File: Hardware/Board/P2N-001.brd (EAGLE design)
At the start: 72 x 72 mm, 34 parts, among them IC1 4053N, IC2 LTC485N, IC3 74LS07N, IC4 LTC485N, K1 G5V1, T1 2SC1815

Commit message: Update document.
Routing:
- net N$22: track 75.4 -> 154.5 mm, vias 5 -> 0
- net N$10: track 143.2 -> 82.9 mm, vias 4 -> 7
- net N$9: track 120.3 -> 61.2 mm, vias 3 -> 2
- net N$11: track 133.1 -> 76.8 mm, vias 3 -> 5
- net N$1: track 61.1 -> 114.4 mm, vias 1 -> 3
- net N$25: track 135.3 -> 86.6 mm, vias 2 -> 3
- net ANLG2: track 95.3 -> 52.4 mm, vias 3 -> 1
- net N$29: track 142.8 -> 107.0 mm, vias 4 -> 2
- net GND: track 333.4 -> 368.5 mm, vias 0 -> 1
- net MIDI11: track 115.8 -> 83.3 mm, vias 2 -> 3
- net N$27: track 53.4 -> 76.1 mm, vias 2 -> 1
- net N$33: track 71.3 -> 92.4 mm, vias 2 -> 4
- net N$28: track 89.5 -> 110.3 mm, vias 3 -> 2
- net ANLG1: track 57.9 -> 78.3 mm, vias 1 -> 3
- net N$19: track 80.7 -> 100.5 mm, vias 2 -> 3
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
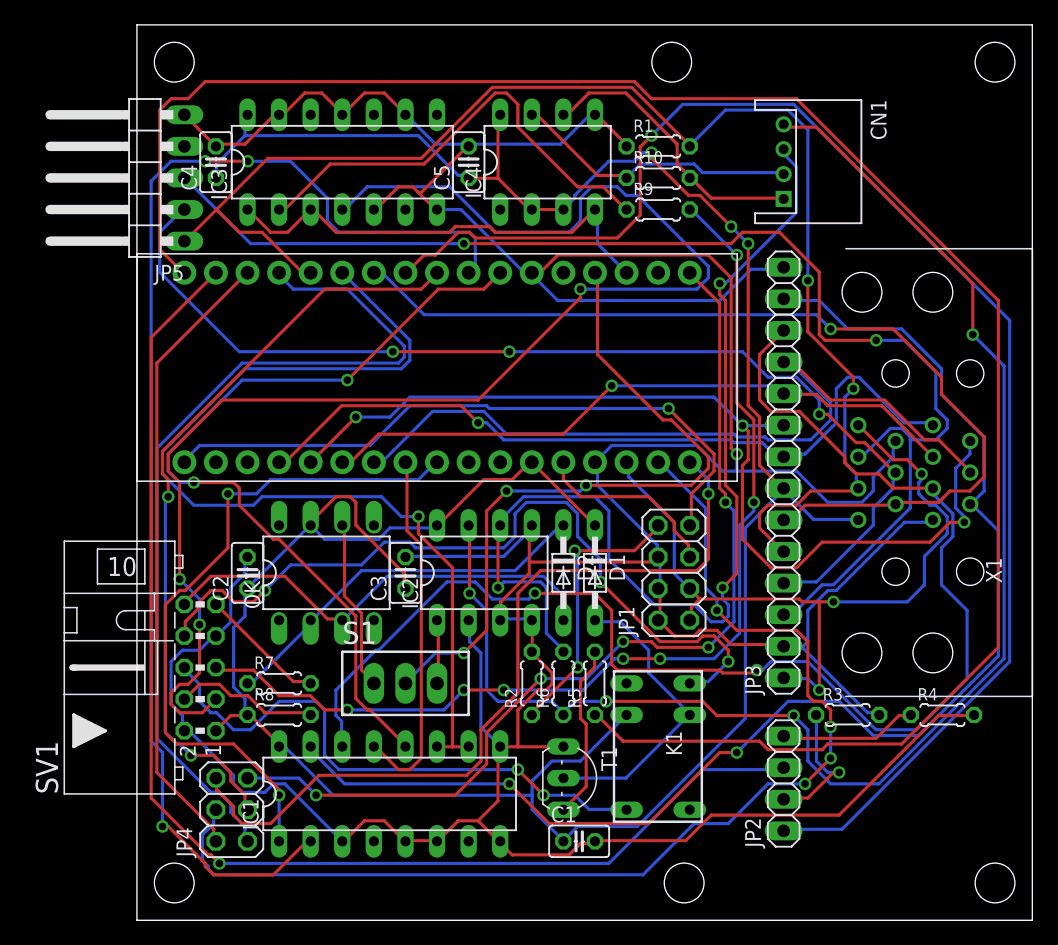
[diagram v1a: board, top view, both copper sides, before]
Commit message: Modified pinout.
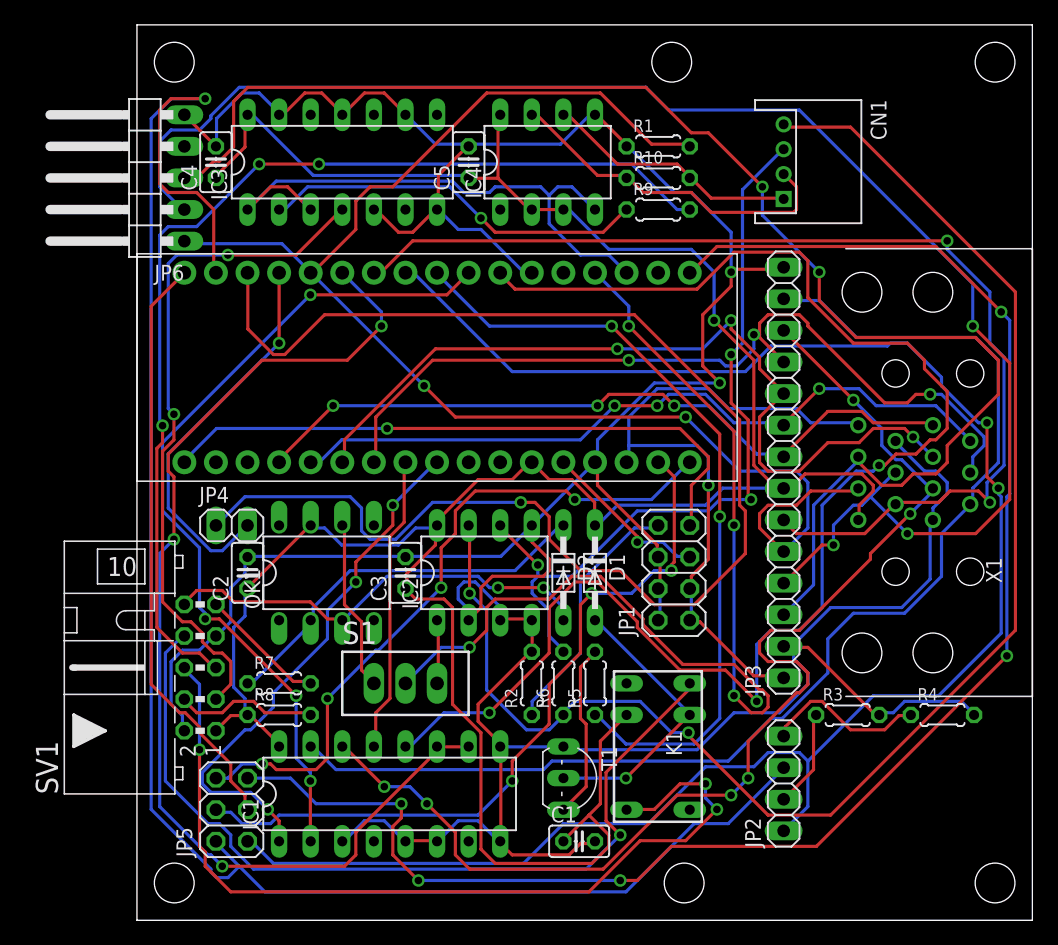
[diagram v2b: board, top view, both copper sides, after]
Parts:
- added JP6: (no value), pinhead:1X05/90
- JP4: device pinhead:2X03 -> pinhead:1X02
- JP5: device pinhead:1X05/90 -> pinhead:2X03
- moved JP5 51.4 mm to (7.62, 8.89)
- moved JP4 22.9 mm to (7.62, 31.8), turned to 0 degrees
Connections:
- removed net N$31: JP4.2, MC1.P$3
- new net N$34: MC1.P$9, R5.1
- net GND: now also JP6.5; no longer JP5.5
- net N$11: now also JP5.5; no longer JP4.5
- net N$13: now also JP5.6; no longer JP4.6
- net N$20: now also JP5.1
- net N$21: now also JP5.2
- net N$22: now also JP4.1, MC1.P$3; no longer MC1.P$1, R5.1
- net N$24: now also JP6.1; no longer JP5.1
- net N$25: now also JP6.2; no longer JP5.2
- net N$26: now also JP6.3; no longer JP5.3
- net N$30: now also JP4.2; no longer JP4.1
- net N$33: now also JP5.4; no longer JP4.4
- net N$9: now also JP5.3, MC1.P$1; no longer JP4.3, MC1.P$9
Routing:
- net N$34: track 0.00 -> 62.8 mm, vias 0 -> 2
- net N$1: track 114.4 -> 55.0 mm, vias 3 -> 2
- net N$11: track 76.8 -> 131.5 mm
- net N$23: track 67.1 -> 119.6 mm, vias 2 -> 3
- net N$31: track 50.8 -> 0.00 mm
- net GND: track 368.5 -> 323.5 mm, vias 1 -> 2
- net N$21: track 100.6 -> 142.4 mm
- net N$22: track 154.5 -> 114.1 mm, vias 0 -> 1
- net N$30: track 71.5 -> 31.3 mm, vias 0 -> 1
- net N$25: track 86.6 -> 126.0 mm
- net N$19: track 100.5 -> 67.9 mm, vias 3 -> 4
- net N$33: track 92.4 -> 60.1 mm, vias 4 -> 3
- net N$20: track 116.2 -> 147.5 mm, vias 1 -> 2
- net N$16: track 45.2 -> 71.0 mm, vias 2 -> 3
- net N$7: track 57.1 -> 81.1 mm, vias 3 -> 4
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
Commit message: Labeled wires.
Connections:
- net GEEK16 renamed SEL
- net MIDI1 renamed TX+
- net MIDI11 renamed RX+
- net MIDI13 renamed RX-
- net MIDI15 renamed RXK
- net MIDI3 renamed TX-
- net MIDI6 renamed TX
- net N$1 renamed RAWTX
- net N$10 renamed RETURN
- net N$11 renamed MOSI
- net N$12 renamed SEND
- net N$13 renamed SCLK
- net N$14 renamed CB
- net N$16 renamed CA
- net N$19 renamed SCL
- net N$20 renamed GPIO0
- net N$21 renamed GPIO1
- net N$22 renamed SX
- net N$23 renamed SDA
- net N$24 renamed PD
- net N$25 renamed USBD-
- net N$26 renamed USBD+
- net N$27 renamed CD
- net N$3 renamed RST
- net N$30 renamed SY
- net N$33 renamed MISO
- net N$34 renamed RELAY
- net N$4 renamed LED
- net N$5 renamed RXA
- net N$7 renamed RX
- net N$9 renamed GPIO2
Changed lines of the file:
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@@
 <via x="27.6606" y="56.4642" extent="1-16" drill="0.6096"/>
 </signal>
-<signal name="MIDI1">
+<signal name="TX+">
 <contactref element="IC4" pad="6"/>
 <contactref element="R10" pad="2"/>
@@
 <wire x1="36.8046" y1="21.4884" x2="36.83" y2="21.59" width="0.254" layer="1"/>
 </signal>
-<signal name="N$1">
+<signal name="RAWTX">
 <contactref element="IC3" pad="4"/>
 <contactref element="SV1" pad="3"/>
@@
 <contactref element="IC1" pad="7"/>
 </signal>
-<signal name="GEEK16">
+<signal name="SEL">
 <contactref element="IC1" pad="11"/>
 <contactref element="IC1" pad="10"/>
@@
 <via x="19.6596" y="47.7774" extent="1-16" drill="0.6096"/>
 </signal>
-<signal name="MIDI6">
+<signal name="TX">
 <contactref element="IC3" pad="1"/>
 <contactref element="IC3" pad="3"/>
@@
 <wire x1="14.1732" y1="24.2316" x2="13.97" y2="24.13" width="0.254" layer="16"/>
 </signal>
-<signal name="MIDI15">
+<signal name="RXK">
 <contactref element="OK1" pad="3"/>
 <contactref element="D2" pad="A"/>
@@
 <via x="29.0322" y="26.7462" extent="1-16" drill="0.6096"/>
 </signal>
-<signal name="MIDI11">
+<signal name="RX+">
 <contactref element="IC2" pad="6"/>
 <contactref element="R6" pad="2"/>
@@
 <via x="32.2326" y="28.575" extent="1-16" drill="0.6096"/>
 </signal>
-<signal name="MIDI13">
+<signal name="RX-">
 <contactref element="IC2" pad="7"/>
 <contactref element="R6" pad="1"/>
@@
 <via x="26.7462" y="26.289" extent="1-16" drill="0.6096"/>
 </signal>
-<signal name="MIDI3">
+<signal name="TX-">
 <contactref element="IC4" pad="7"/>
 <contactref element="R10" pad="1"/>
@@
 <wire x1="39.3192" y1="59.8932" x2="39.37" y2="59.69" width="0.254" layer="1"/>
 </signal>
-<signal name="N$3">
+<signal name="RST">
 <contactref element="JP1" pad="5"/>
 <contactref element="MC1" pad="P$13"/>
@@
 <via x="40.2336" y="30.4038" extent="1-16" drill="0.6096"/>
 </signal>
-<signal name="N$4">
+<signal name="LED">
 <contactref element="JP1" pad="7"/>
 <contactref element="MC1" pad="P$34"/>
@@
 <via x="20.574" y="33.3756" extent="1-16" drill="0.6096"/>
 </signal>
-<signal name="N$10">
+<signal name="RETURN">
 <contactref element="R9" pad="2"/>
 <contactref element="SV1" pad="5"/>
@@
 <via x="2.0574" y="39.7764" extent="1-16" drill="0.6096"/>
 </signal>
-<signal name="N$12">
+<signal name="SEND">
 <contactref element="R8" pad="2"/>
 <contactref element="SV1" pad="4"/>
@@
 <wire x1="3.8862" y1="17.6022" x2="3.81" y2="17.78" width="0.254" layer="1"/>
 </signal>
-<signal name="N$14">
+<signal name="CB">
 <contactref element="K1" pad="10"/>
 <contactref element="SV1" pad="8"/>
@@
 <via x="38.862" y="6.858" extent="1-16" drill="0.6096"/>
 </signal>
-<signal name="N$16">
+<signal name="CA">
 <contactref element="K1" pad="5"/>
 <contactref element="SV1" pad="6"/>
@@
 <via x="5.0292" y="13.716" extent="1-16" drill="0.6096"/>
 </signal>
-<signal name="N$20">
+<signal name="GPIO0">
 <contactref element="MC1" pad="P$8"/>
 <contactref element="JP2" pad="1"/>
@@
 <via x="69.2658" y="34.7472" extent="1-16" drill="0.6096"/>
 </signal>
-<signal name="N$21">
+<signal name="GPIO1">
 <contactref element="MC1" pad="P$2"/>
 <contactref element="JP2" pad="3"/>
@@
 <via x="5.4864" y="66.0654" extent="1-16" drill="0.6096"/>
 </signal>
-<signal name="N$19">
+<signal name="SCL">
 <contactref element="IC1" pad="2"/>
 <contactref element="MC1" pad="P$10"/>
@@
 <via x="13.9446" y="50.292" extent="1-16" drill="0.6096"/>
 </signal>
-<signal name="N$23">
+<signal name="SDA">
 <contactref element="MC1" pad="P$11"/>
 <contactref element="IC1" pad="12"/>
@@
 <via x="59.6646" y="36.576" extent="1-16" drill="0.6096"/>
 </signal>
-<signal name="N$24">
+<signal name="PD">
 <contactref element="X1" pad="5"/>
 <contactref element="JP6" pad="1"/>
@@
 <via x="23.0886" y="42.9768" extent="1-16" drill="0.6096"/>
 </signal>
-<signal name="N$25">
+<signal name="USBD-">
 <contactref element="X1" pad="4"/>
 <contactref element="JP6" pad="2"/>
@@
 <via x="61.9506" y="31.0896" extent="1-16" drill="0.6096"/>
 </signal>
-<signal name="N$26">
+<signal name="USBD+">
 <contactref element="X1" pad="3"/>
 <contactref element="JP6" pad="3"/>
@@
 <via x="54.864" y="52.1208" extent="1-16" drill="0.6096"/>
 </signal>
-<signal name="N$27">
+<signal name="CD">
 <contactref element="X1" pad="6"/>
 <contactref element="JP3" pad="6"/>
@@
 <wire x1="41.8338" y1="31.5468" x2="41.91" y2="31.75" width="0.254" layer="16"/>
 </signal>
-<signal name="N$5">
+<signal name="RXA">
 <contactref element="R7" pad="2"/>
 <contactref element="SV1" pad="9"/>
@@
 <wire x1="6.4008" y1="25.3746" x2="6.35" y2="25.4" width="0.254" layer="1"/>
 </signal>
-<signal name="N$7">
+<signal name="RX">
 <contactref element="S1" pad="2"/>
 <contactref element="MC1" pad="P$14"/>
@@
 <via x="39.5478" y="47.7774" extent="1-16" drill="0.6096"/>
 </signal>
-<signal name="N$13">
+<signal name="SCLK">
 <contactref element="MC1" pad="P$18"/>
 <contactref element="JP5" pad="6"/>
@@
 <via x="35.2044" y="33.8328" extent="1-16" drill="0.6096"/>
 </signal>
-<signal name="N$33">
+<signal name="MISO">
 <contactref element="MC1" pad="P$19"/>
 <contactref element="JP5" pad="4"/>
@@
 <via x="42.9768" y="28.1178" extent="1-16" drill="0.6096"/>
 </signal>
-<signal name="N$11">
+<signal name="MOSI">
 <contactref element="JP5" pad="5"/>
 <contactref element="MC1" pad="P$17"/>
@@
 <via x="69.4944" y="48.9204" extent="1-16" drill="0.6096"/>
 </signal>
-<signal name="N$34">
+<signal name="RELAY">
 <contactref element="R5" pad="1"/>
 <contactref element="MC1" pad="P$9"/>
@@
 <via x="38.1762" y="47.7774" extent="1-16" drill="0.6096"/>
 </signal>
-<signal name="N$9">
+<signal name="GPIO2">
 <contactref element="MC1" pad="P$1"/>
 <contactref element="JP5" pad="3"/>
@@
 <wire x1="3.6576" y1="51.8922" x2="3.81" y2="52.07" width="0.254" layer="1"/>
 </signal>
-<signal name="N$22">
+<signal name="SX">
 <contactref element="JP4" pad="1"/>
 <contactref element="MC1" pad="P$3"/>
@@
 <via x="30.861" y="33.6042" extent="1-16" drill="0.6096"/>
 </signal>
-<signal name="N$30">
+<signal name="SY">
 <contactref element="JP4" pad="2"/>
 <contactref element="MC1" pad="P$4"/>

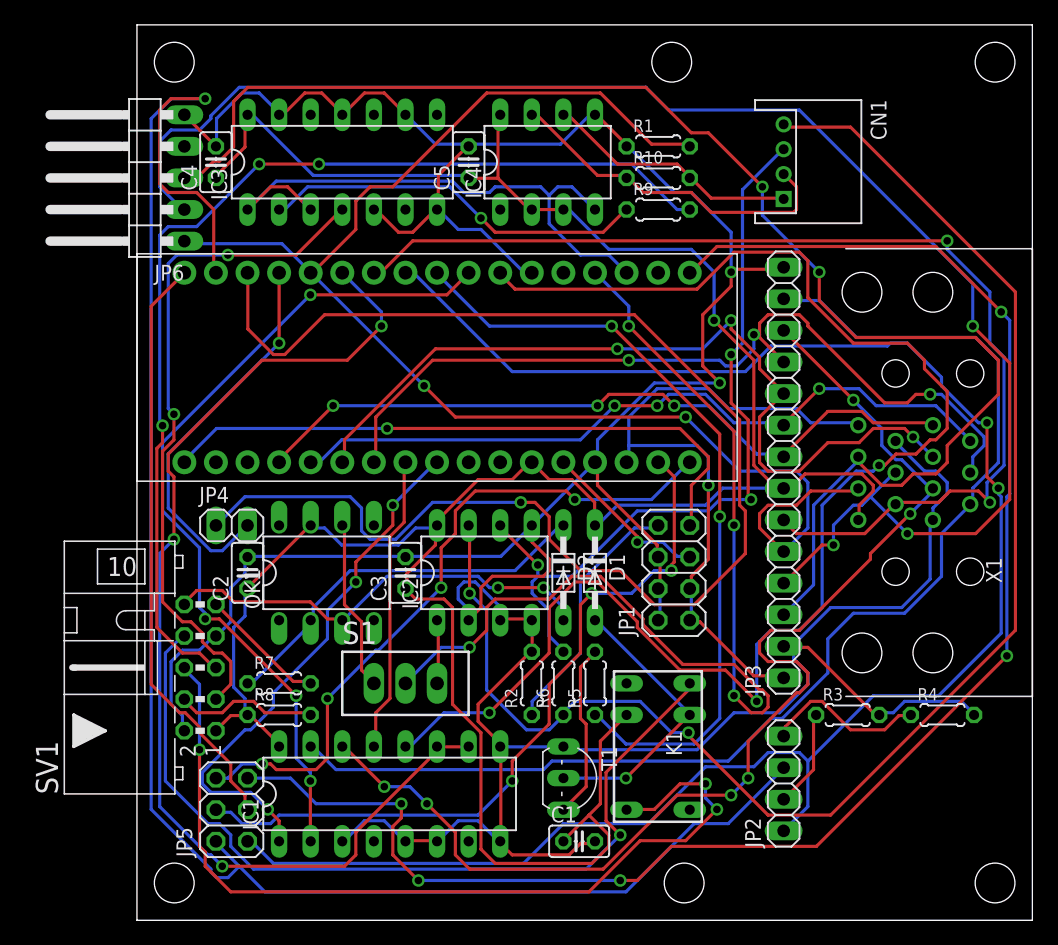
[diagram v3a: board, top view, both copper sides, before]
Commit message: Added anther LED pattern.
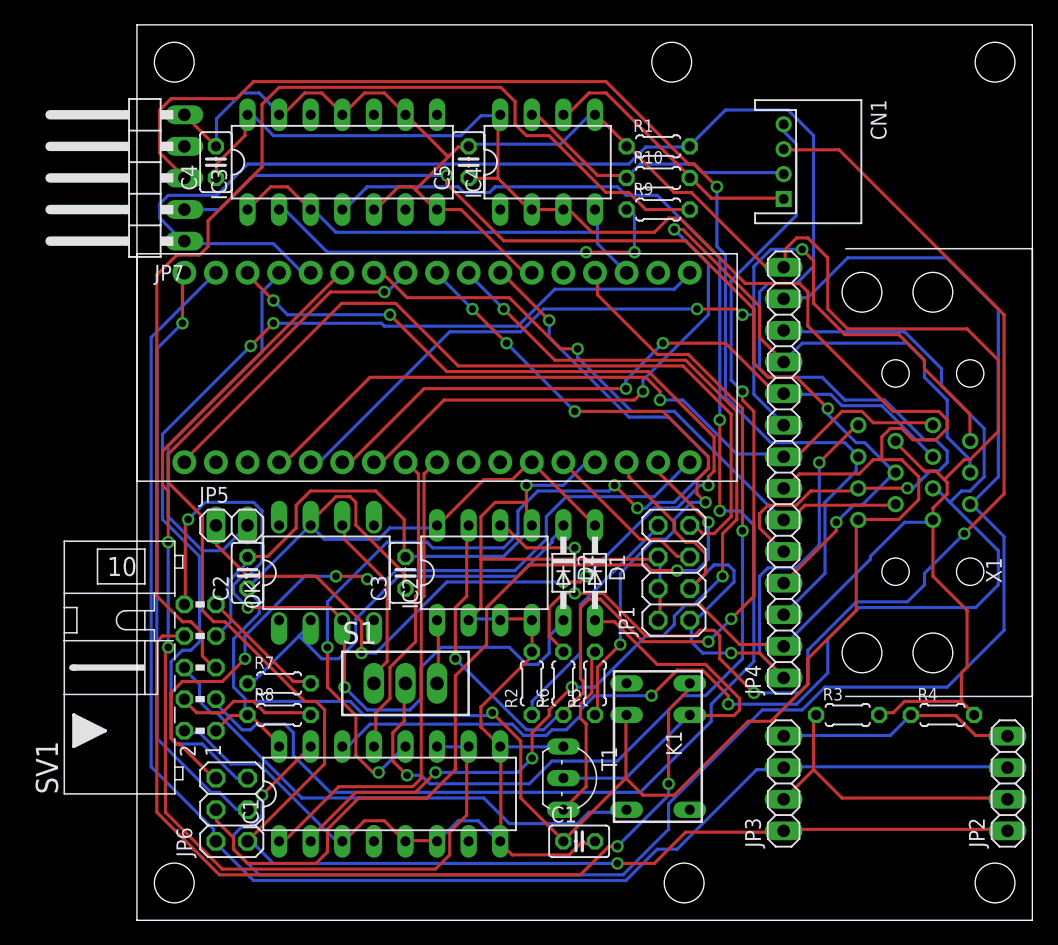
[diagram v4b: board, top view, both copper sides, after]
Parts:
- added JP7: (no value), pinhead:1X05/90
- JP3: device pinhead:1X14 -> pinhead:1X04
- JP4: device pinhead:1X02 -> pinhead:1X14
- JP5: device pinhead:2X03 -> pinhead:1X02
- JP6: device pinhead:1X05/90 -> pinhead:2X03
- moved JP6 51.4 mm to (7.62, 8.89)
- moved JP4 44.6 mm to (52.0, 36.0), turned to 90 degrees
- moved JP3 25.0 mm to (52.0, 11.0)
- moved JP5 22.9 mm to (7.62, 31.8), turned to 0 degrees
- moved JP2 18.0 mm to (70.0, 11.0)
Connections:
- net ANLG0: now also JP4.8; no longer JP3.8
- net ANLG1: now also JP4.9; no longer JP3.9
- net ANLG2: now also JP4.10; no longer JP3.10
- net ANLG3: now also JP4.11; no longer JP3.11
- net CD: now also JP4.6; no longer JP3.6
- net GND: now also JP4.14, JP4.2, JP7.5; no longer JP3.14, JP3.2, JP6.5
- net GPIO0: now also JP3.1, JP6.1; no longer JP5.1
- net GPIO1: now also JP3.3, JP6.2; no longer JP5.2
- net GPIO2: now also JP6.3; no longer JP5.3
- net MISO: now also JP6.4; no longer JP5.4
- net MOSI: now also JP6.5; no longer JP5.5
- net N$17: now also JP3.2
- net N$18: now also JP3.4
- net N$28: now also JP4.12; no longer JP3.12
- net N$29: now also JP4.13; no longer JP3.13
- net PD: now also JP4.5, JP7.1; no longer JP3.5, JP6.1
- net SCLK: now also JP6.6; no longer JP5.6
- net SX: now also JP5.1; no longer JP4.1
- net SY: now also JP5.2; no longer JP4.2
- net USBD+: now also JP4.3, JP7.3; no longer JP3.3, JP6.3
- net USBD-: now also JP4.4, JP7.2; no longer JP3.4, JP6.2
- net VCC: now also JP4.7; no longer JP3.7
- net VDD: now also JP4.1; no longer JP3.1
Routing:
- net RAWTX: track 55.0 -> 121.7 mm
- net MOSI: track 131.5 -> 82.5 mm, vias 5 -> 2
- net VCC: track 214.7 -> 257.7 mm
- net USBD-: track 126.0 -> 84.5 mm
- net RX+: track 62.9 -> 102.7 mm, vias 3 -> 4
- net CD: track 89.6 -> 51.1 mm, vias 2 -> 1
- net SDA: track 119.6 -> 81.4 mm, vias 3 -> 5
- net N$29: track 98.1 -> 131.7 mm, vias 0 -> 1
- net RX-: track 120.3 -> 90.6 mm, vias 2 -> 4
- net CA: track 71.0 -> 42.2 mm, vias 3 -> 0
- net RXK: track 35.5 -> 61.5 mm, vias 2 -> 3
- net GPIO1: track 142.4 -> 118.9 mm, vias 1 -> 0
- net ANLG1: track 59.4 -> 82.7 mm
- net GPIO0: track 147.5 -> 128.3 mm
- net N$17: track 7.94 -> 24.5 mm
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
